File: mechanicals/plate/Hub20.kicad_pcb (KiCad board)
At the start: 4 copper layers, 89 x 124 mm, 4 parts

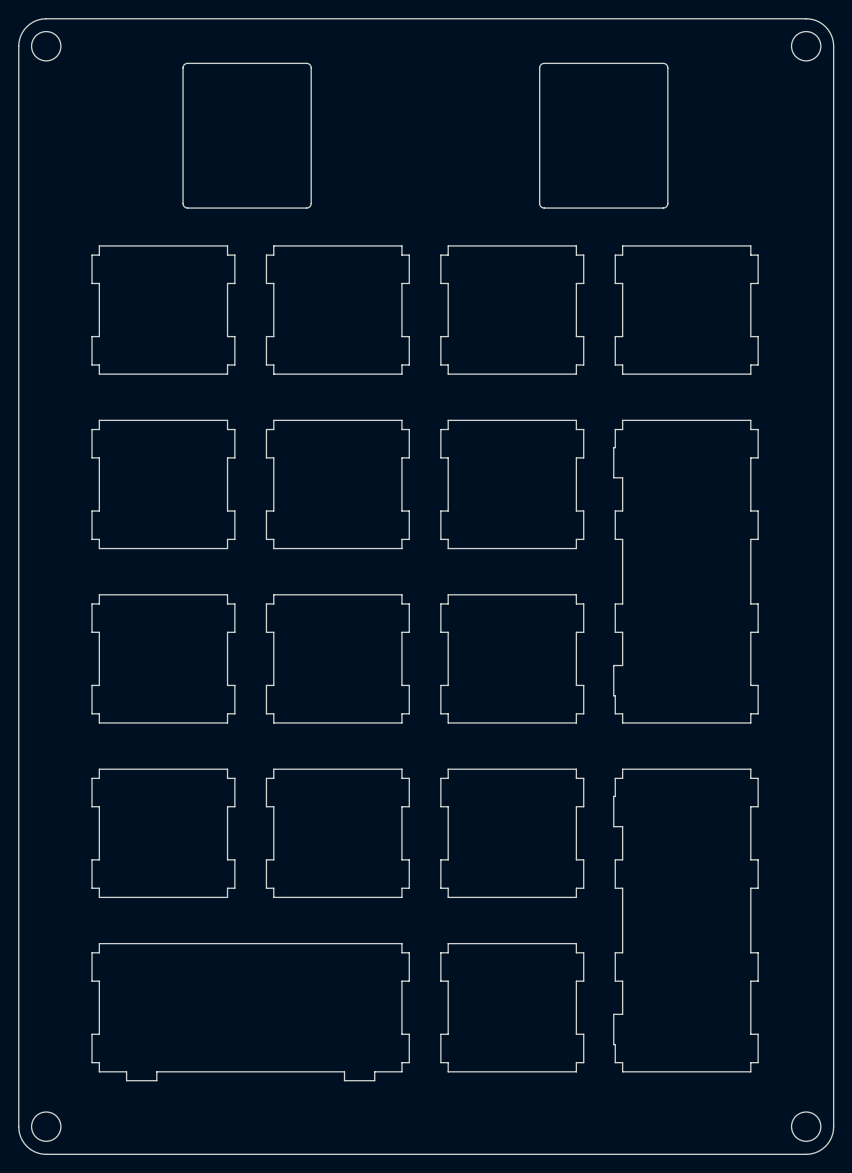
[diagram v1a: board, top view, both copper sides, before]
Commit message: limit 2U to 3 pin only
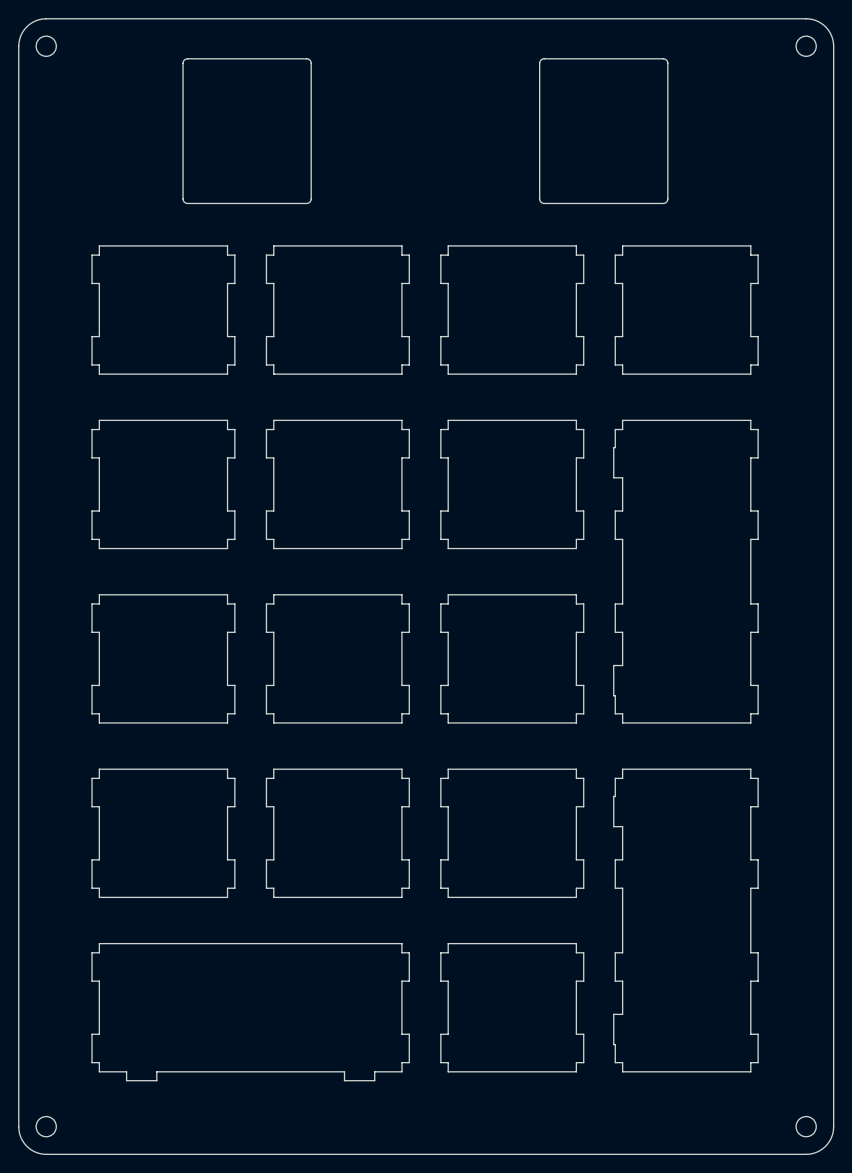
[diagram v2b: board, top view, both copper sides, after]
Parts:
- H1, H2, H3, H4: footprint MountingHole:MountingHole_3.2mm_M3 -> MountingHole:MountingHole_2.2mm_M2
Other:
- outline, holes or cut-outs redrawn
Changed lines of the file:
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@@
-(kicad_pcb (version 20171130) (host pcbnew 5.1.6-c6e7f7d~87~ubuntu20.04.1)
+(kicad_pcb (version 20171130) (host pcbnew "(5.1.5)-3")
   (general
     (thickness 1.6)
@@
     (diff_pair_gap 0.2)
   )
-  (module MountingHole:MountingHole_3.2mm_M3 locked (layer F.Cu)
+  (module MountingHole:MountingHole_2.2mm_M2 locked (layer F.Cu)
     (at 180.45 157.5375)
-    (descr "Mounting Hole 3.2mm, no annular, M3")
-    (tags "mounting hole 3.2mm no annular m3")
+    (descr "Mounting Hole 2.2mm, no annular, M2")
+    (tags "mounting hole 2.2mm no annular m2")
     (attr virtual)
     (fp_text reference H3 (at 0 -4.2) (layer F.SilkS) hide
@@
       (effects (font (size 1 1) (thickness 0.15)))
     )
-    (fp_circle (center 0 0) (end 3.45 0) (layer F.CrtYd) (width 0.05))
-    (fp_circle (center 0 0) (end 3.2 0) (layer Cmts.User) (width 0.15))
+    (fp_circle (center 0 0) (end 2.45 0) (layer F.CrtYd) (width 0.05))
+    (fp_circle (center 0 0) (end 2.2 0) (layer Cmts.User) (width 0.15))
     (fp_text user %R (at 0.3 0) (layer F.Fab) hide
       (effects (font (size 1 1) (thickness 0.15)))
     )
-    (pad 1 np_thru_hole circle (at 0 0) (size 3.2 3.2) (drill 3.2) (layers *.Cu *.Mask))
-  )
-  (module MountingHole:MountingHole_3.2mm_M3 locked (layer F.Cu)
+    (pad 1 np_thru_hole circle (at 0 0) (size 2.2 2.2) (drill 2.2) (layers *.Cu *.Mask))
+  )
+  (module MountingHole:MountingHole_2.2mm_M2 locked (layer F.Cu)
     (at 97.45 157.5375)
-    (descr "Mounting Hole 3.2mm, no annular, M3")
-    (tags "mounting hole 3.2mm no annular m3")
+    (descr "Mounting Hole 2.2mm, no annular, M2")
+    (tags "mounting hole 2.2mm no annular m2")
     (attr virtual)
     (fp_text reference H4 (at 0 -4.2) (layer F.SilkS) hide
@@
       (effects (font (size 1 1) (thickness 0.15)))
     )
-    (fp_circle (center 0 0) (end 3.45 0) (layer F.CrtYd) (width 0.05))
-    (fp_circle (center 0 0) (end 3.2 0) (layer Cmts.User) (width 0.15))
+    (fp_circle (center 0 0) (end 2.45 0) (layer F.CrtYd) (width 0.05))
+    (fp_circle (center 0 0) (end 2.2 0) (layer Cmts.User) (width 0.15))
     (fp_text user %R (at 0.3 0) (layer F.Fab) hide
       (effects (font (size 1 1) (thickness 0.15)))
     )
-    (pad 1 np_thru_hole circle (at 0 0) (size 3.2 3.2) (drill 3.2) (layers *.Cu *.Mask))
-  )
-  (module MountingHole:MountingHole_3.2mm_M3 locked (layer F.Cu)
+    (pad 1 np_thru_hole circle (at 0 0) (size 2.2 2.2) (drill 2.2) (layers *.Cu *.Mask))
+  )
+  (module MountingHole:MountingHole_2.2mm_M2 locked (layer F.Cu)
     (at 180.45 39.5375 90)
-    (descr "Mounting Hole 3.2mm, no annular, M3")
-    (tags "mounting hole 3.2mm no annular m3")
+    (descr "Mounting Hole 2.2mm, no annular, M2")
+    (tags "mounting hole 2.2mm no annular m2")
     (attr virtual)
     (fp_text reference H1 (at 0 -4.2 90) (layer F.SilkS) hide
@@
       (effects (font (size 1 1) (thickness 0.15)))
     )
-    (fp_circle (center 0 0) (end 3.2 0) (layer Cmts.User) (width 0.15))
-    (fp_circle (center 0 0) (end 3.45 0) (layer F.CrtYd) (width 0.05))
+    (fp_circle (center 0 0) (end 2.45 0) (layer F.CrtYd) (width 0.05))
+    (fp_circle (center 0 0) (end 2.2 0) (layer Cmts.User) (width 0.15))
     (fp_text user %R (at 0.3 0 90) (layer F.Fab) hide
       (effects (font (size 1 1) (thickness 0.15)))
     )
-    (pad 1 np_thru_hole circle (at 0 0 90) (size 3.2 3.2) (drill 3.2) (layers *.Cu *.Mask))
-  )
-  (module MountingHole:MountingHole_3.2mm_M3 locked (layer F.Cu)
+    (pad 1 np_thru_hole circle (at 0 0 90) (size 2.2 2.2) (drill 2.2) (layers *.Cu *.Mask))
+  )
+  (module MountingHole:MountingHole_2.2mm_M2 locked (layer F.Cu)
     (at 97.45 39.5375)
-    (descr "Mounting Hole 3.2mm, no annular, M3")
-    (tags "mounting hole 3.2mm no annular m3")
+    (descr "Mounting Hole 2.2mm, no annular, M2")
+    (tags "mounting hole 2.2mm no annular m2")
     (attr virtual)
     (fp_text reference H2 (at 0 -4.2) (layer F.SilkS) hide
@@
       (effects (font (size 1 1) (thickness 0.15)))
     )
-    (fp_circle (center 0 0) (end 3.2 0) (layer Cmts.User) (width 0.15))
-    (fp_circle (center 0 0) (end 3.45 0) (layer F.CrtYd) (width 0.05))
+    (fp_circle (center 0 0) (end 2.45 0) (layer F.CrtYd) (width 0.05))
+    (fp_circle (center 0 0) (end 2.2 0) (layer Cmts.User) (width 0.15))
     (fp_text user %R (at 0.3 0) (layer F.Fab) hide
       (effects (font (size 1 1) (thickness 0.15)))
     )
-    (pad 1 np_thru_hole circle (at 0 0) (size 3.2 3.2) (drill 3.2) (layers *.Cu *.Mask))
+    (pad 1 np_thru_hole circle (at 0 0) (size 2.2 2.2) (drill 2.2) (layers *.Cu *.Mask))
   )
   (gr_line (start 160.4013 150.54849) (end 160.4013 151.54896) (layer Edge.Cuts) (width 0.05))
@@
   (gr_line (start 174.4006 81.4) (end 174.4006 80.3995) (layer Edge.Cuts) (width 0.05))
   (gr_line (start 175.2 81.4) (end 174.4006 81.4) (layer Edge.Cuts) (width 0.05))
-  (gr_line (start 165.34 41.91) (end 165.34 56.709999) (layer Edge.Cuts) (width 0.05))
-  (gr_line (start 151.84 41.41) (end 164.84 41.41) (layer Edge.Cuts) (width 0.05))
-  (gr_arc (start 125.89 41.91) (end 126.39 41.91) (angle -90) (layer Edge.Cuts) (width 0.05))
-  (gr_arc (start 151.84 56.709999) (end 151.34 56.709999) (angle -90) (layer Edge.Cuts) (width 0.05))
-  (gr_arc (start 112.89 41.91) (end 112.89 41.41) (angle -90) (layer Edge.Cuts) (width 0.05))
-  (gr_arc (start 164.84 56.709999) (end 164.84 57.209999) (angle -90) (layer Edge.Cuts) (width 0.05))
-  (gr_arc (start 164.84 41.91) (end 165.34 41.91) (angle -90) (layer Edge.Cuts) (width 0.05))
-  (gr_line (start 126.39 41.91) (end 126.39 56.709999) (layer Edge.Cuts) (width 0.05))
-  (gr_arc (start 151.84 41.91) (end 151.84 41.41) (angle -90) (layer Edge.Cuts) (width 0.05))
-  (gr_arc (start 125.89 56.709999) (end 125.89 57.209999) (angle -90) (layer Edge.Cuts) (width 0.05))
-  (gr_arc (start 112.89 56.709999) (end 112.39 56.709999) (angle -90) (layer Edge.Cuts) (width 0.05))
-  (gr_line (start 112.39 41.91) (end 112.39 56.709999) (layer Edge.Cuts) (width 0.05))
-  (gr_line (start 112.89 57.209999) (end 125.89 57.209999) (layer Edge.Cuts) (width 0.05))
-  (gr_line (start 151.34 41.91) (end 151.34 56.709999) (layer Edge.Cuts) (width 0.05))
-  (gr_line (start 151.84 57.209999) (end 164.84 57.209999) (layer Edge.Cuts) (width 0.05))
-  (gr_line (start 112.89 41.41) (end 125.89 41.41) (layer Edge.Cuts) (width 0.05))
+  (gr_line (start 165.34 41.41) (end 165.34 56.209999) (layer Edge.Cuts) (width 0.05))
+  (gr_line (start 151.84 40.91) (end 164.84 40.91) (layer Edge.Cuts) (width 0.05))
+  (gr_arc (start 125.89 41.41) (end 126.39 41.41) (angle -90) (layer Edge.Cuts) (width 0.05))
+  (gr_arc (start 151.84 56.209999) (end 151.34 56.209999) (angle -90) (layer Edge.Cuts) (width 0.05))
+  (gr_arc (start 112.89 41.41) (end 112.89 40.91) (angle -90) (layer Edge.Cuts) (width 0.05))
+  (gr_arc (start 164.84 56.209999) (end 164.84 56.709999) (angle -90) (layer Edge.Cuts) (width 0.05))
+  (gr_arc (start 164.84 41.41) (end 165.34 41.41) (angle -90) (layer Edge.Cuts) (width 0.05))
+  (gr_line (start 126.39 41.41) (end 126.39 56.209999) (layer Edge.Cuts) (width 0.05))
+  (gr_arc (start 151.84 41.41) (end 151.84 40.91) (angle -90) (layer Edge.Cuts) (width 0.05))
+  (gr_arc (start 125.89 56.209999) (end 125.89 56.709999) (angle -90) (layer Edge.Cuts) (width 0.05))
+  (gr_arc (start 112.89 56.209999) (end 112.39 56.209999) (angle -90) (layer Edge.Cuts) (width 0.05))
+  (gr_line (start 112.39 41.41) (end 112.39 56.209999) (layer Edge.Cuts) (width 0.05))
+  (gr_line (start 112.89 56.709999) (end 125.89 56.709999) (layer Edge.Cuts) (width 0.05))
+  (gr_line (start 151.34 41.41) (end 151.34 56.209999) (layer Edge.Cuts) (width 0.05))
+  (gr_line (start 151.84 56.709999) (end 164.84 56.709999) (layer Edge.Cuts) (width 0.05))
+  (gr_line (start 112.89 40.91) (end 125.89 40.91) (layer Edge.Cuts) (width 0.05))
   (gr_line (start 94.45 157.5625) (end 94.45 39.5375) (layer Edge.Cuts) (width 0.1))
   (gr_line (start 183.45 157.5625) (end 183.45 39.5375) (layer Edge.Cuts) (width 0.1))
